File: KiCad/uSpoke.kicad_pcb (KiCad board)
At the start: 2 copper layers, 30 x 50 mm, 67 parts, among them J12 Amphenol 132289, J2 PLS-1x3, J4 PLS-1x3, Q2 AO3407A, Q3 AO3400, Q5 AO3400, U1 SP0503BAHTG, U2 TP4056, U4 LM3671MF-3.3, U5 74HC4052PW, U6 STM32F103C8T6, X1 8MHz

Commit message: Update PCB
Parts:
- removed SW5: ~, Spoke:Button_6x6
- added J1: SM12B-SRSS-TB, uSpoke:SM12B-SRSS-TB, F.Cu at (187.8, 97.5)
- added SW4: SW-SPST-2P, uSpoke:TL3330AF260QG, F.Cu at (193.4, 73.5)
- added TP1: Pad-Round, uSpoke:Pad_round, F.Cu at (161.5, 77.5)
- added TP2: Pad-Round, uSpoke:Pad_round, F.Cu at (161.5, 81.1)
- added TP3: Pad-Round, uSpoke:Pad_round, F.Cu at (161.5, 84.7)
- A1: footprint Spoke:E104-BT5005A -> uSpoke:E104-BT5005A
- A2: footprint Spoke:E22 -> uSpoke:E22
- C1, C13, C5, C8: footprint Spoke:C1206 -> uSpoke:C0805
- C11, C15, C16, C17, C18, C19, C20, C22, C23, C27, C30: footprint Spoke:C0603 -> uSpoke:C0603
- C14, C25, C26, C28: footprint Spoke:C_tantA -> uSpoke:C_tantA
- D1, D3, Q2, Q3: footprint Spoke:SOT-23 -> uSpoke:SOT-23
- D2, D4, D5: footprint Spoke:LED_3mm -> uSpoke:LED0603; moved to F.Cu
- J12: footprint Spoke:SMA -> uSpoke:SMA
- J2: value PLS-1x3 -> PLS-1x4; footprint Spoke:Header_1x3 -> uSpoke:Header_1x4
- J4: footprint Spoke:Header_1x3 -> uSpoke:Header_1x3
- L1: footprint Spoke:L1616 -> uSpoke:L1616
- Q5: footprint Spoke:SOT-23 -> uSpoke:SOT-23; moved to F.Cu
- R1, R10, R11, R12, R13, R17, R23, R26, R27, R28, R29, R3, R32, R33, R34, R5, R6, R7, R8, R9: footprint Spoke:R0603 -> uSpoke:R0603
- R15: footprint Spoke:R0603 -> uSpoke:R0603; moved to F.Cu
- R4: value 3.9kR -> 2.0kR; footprint Spoke:R0603 -> uSpoke:R0603
- SW1, SW2, SW3: value ~ -> SW-SPST-2P; footprint Spoke:Button_6x6 -> uSpoke:TL3330AF260QG
- TP10, TP11: footprint Spoke:Pad_round -> uSpoke:Pad_round
- U1: footprint Spoke:SOT-23-5 -> uSpoke:SOT-143
- U2: value TP4056 -> MCP73831T-2ACI/OT; footprint Spoke:SOIC-8-EP -> uSpoke:SOT-23-5
- U4: footprint Spoke:SOT-23-5 -> uSpoke:SOT-23-5
- U5: footprint Spoke:TSSOP-16 -> uSpoke:TSSOP-16
- U6: footprint Spoke:LQFP-48 -> uSpoke:LQFP-48
- X1: footprint Spoke:Xtal_3225 -> uSpoke:Xtal_3225
- moved SW1 197.9 mm to (193.5, 64.3), turned to 90 degrees
- moved R12 195.5 mm to (174.5, 111.0), turned to 180 degrees
- moved SW2 193.3 mm to (193.5, 55.1), turned to 90 degrees
- moved SW3 170.3 mm to (175.4, 20.6)
- moved R3 157.2 mm to (199.5, 67.6)
- moved R5 157.2 mm to (199.5, 70.2)
- moved C28 144.0 mm to (188.5, 108.1)
- moved C30 144.0 mm to (191.0, 108.8)
- moved R6 140.7 mm to (182.8, 85.2), turned to -90 degrees
- moved R1 139.0 mm to (174.5, 109.5)
- moved J2 122.6 mm to (167.1, 95.1), turned to 90 degrees
- moved R15 106.1 mm to (184.9, 92.5), turned to -90 degrees
- moved Q5 100.8 mm to (174.3, 106.7)
- moved D5 69.6 mm to (189.6, 53.2), turned to -90 degrees
- moved D4 63.6 mm to (188.1, 53.2), turned to -90 degrees
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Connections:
- C28 pad 1: BUZZ_P -> unconnected-(C28-Pad1)
- C28 pad 2: GND -> unconnected-(C28-Pad2)
- C30 pad 1: BUZZ_P -> unconnected-(C30-Pad1)
- C30 pad 2: GND -> unconnected-(C30-Pad2)
- J2 pad 1: CONSOLE_TXD_EXT -> unconnected-(J2-Pad1)
- J2 pad 2: CONSOLE_RXD_EXT -> unconnected-(J2-Pad2)
- J2 pad 3: GND -> unconnected-(J2-Pad3)
- R4 pad 1: GND -> Net-(U2-PROG)
- R4 pad 2: Net-(U2-PROG) -> GND
- SW1 pad 1: Net-(D1-Pad3) -> BUZZ_P
- SW1 pad 2: Net-(D1-Pad3) -> unconnected-(SW1-Pad2)
- SW1 pad 3: GND -> unconnected-(SW1-1-Pad3)
- SW1 pad 4: GND -> BOOT0
- SW2 pad 2: BTN_OK -> GND
- SW2 pad 3: GND -> unconnected-(SW2-1-Pad3)
- SW2 pad 4: GND -> unconnected-(SW2-1-Pad4)
- SW3 pad 2: BTN_ESC -> GND
- SW3 pad 3: GND -> unconnected-(SW3-1-Pad3)
- SW3 pad 4: GND -> unconnected-(SW3-1-Pad4)
- U1 pad 1: GND -> unconnected-(U1-A-Pad1)
- U1 pad 2: CONSOLE_TXD_EXT -> unconnected-(U1-K-Pad2)
- U1 pad 3: CONSOLE_RXD_EXT -> unconnected-(U1-K-Pad3)
- U1 pad 4: VEXT -> unconnected-(U1-K-Pad4)
- U2 pad 1: GND -> Net-(D2-K)
- U2 pad 2: Net-(U2-PROG) -> GND
- U2 pad 3: GND -> +BATT
- U2 pad 5: +BATT -> Net-(U2-PROG)
- U6 pad 42: unconnected-(U6-PB6-Pad42) -> I2C_SCL
- U6 pad 43: unconnected-(U6-PB7-Pad43) -> I2C_SDA
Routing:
- removed copper zone on B.Cu, net /ANT
- removed copper zone on F.Cu, net BUZZ_P
- removed copper zone on B.Cu, net VEXT
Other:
- board text removed: "+"
- board text removed: "-"
- board text removed: "B+"
- board text removed: "B-"
- board text removed: "CL"
- board text removed: "G"
- board text removed: "IO"
- board text removed: "RS"
- board text removed: "RX"
- board text removed: "TX"
- board text removed: "V"
- board text removed: "V+"
- board text removed: "V-"
- board text removed: "boot"

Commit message: Color 12P conn
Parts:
- J1: value SM12B-SRSS-TB -> Untitled
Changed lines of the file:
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@@
 		(at 184.95 92.47 -90)
 		(property "Reference" "R15"
-			(at 0 -1.43 -90)
+			(at 0 -1.43 270)
 			(layer "F.SilkS")
 			(effects
@@
 		)
 		(property "Value" "100kR"
-			(at 0 1.43 -90)
+			(at 0 1.43 270)
 			(layer "F.Fab")
 			(effects
@@
 		)
 		(property "Datasheet" ""
-			(at 0 0 -90)
+			(at 0 0 270)
 			(layer "F.Fab")
 			(hide yes)
@@
 		)
 		(property "Description" ""
-			(at 0 0 -90)
+			(at 0 0 270)
 			(layer "F.Fab")
 			(hide yes)
@@
 			)
 		)
-		(property "Value" "SM12B-SRSS-TB"
+		(property "Value" "Untitled"
 			(at 0.2 8.9 0)
 			(unlocked yes)

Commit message: SCH to PCB sync
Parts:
- removed C20, C22, C23, C27, C30: 100nF, uSpoke:C0603
- removed C25, C26, C28: 47uF, uSpoke:C_tantA
- removed J12: Amphenol 132289, uSpoke:SMA
- removed Q5: AO3400, uSpoke:SOT-23
- removed R23, R28, R32, R33, R34: 100kR, uSpoke:R0603
- removed R26, R27, R29: 1kR, uSpoke:R0603
- removed SW4: SW-SPST-2P, uSpoke:TL3330AF260QG
- removed TP10, TP11: Pad-Round, uSpoke:Pad_round
- removed U6: STM32F103C8T6, uSpoke:LQFP-48
- added C10: 100nF, uSpoke:C0603, F.Cu at (123.5, 60.8)
- added C12: 100nF, uSpoke:C0603, F.Cu at (123.5, 63.4)
- added C2: 47uF, uSpoke:C_tantA, F.Cu at (134.1, 75.1)
- added C3: 10uF, uSpoke:C0805, F.Cu at (132.5, 58.4)
- added C4: 10uF, uSpoke:C0805, F.Cu at (132.5, 61.4)
- added C6: 10uF, uSpoke:C0805, F.Cu at (132.5, 64.4)
- added C7: 10uF, uSpoke:C0805, F.Cu at (132.5, 67.4)
- added C9: 12pF, uSpoke:C0603, F.Cu at (123.5, 58.2)
- added J3: PLS-1x3, uSpoke:Header_1x3, F.Cu at (135.4, 71.0)
- added Q1: AO3407A, uSpoke:SOT-23, F.Cu at (140.1, 75.8)
- added R14: 1kR, uSpoke:R0603, F.Cu at (123.5, 68.6)
- added R16: 100kR, uSpoke:R0603, F.Cu at (123.5, 71.2)
- added R18: 100kR, uSpoke:R0603, F.Cu at (127.9, 58.2)
- added R19: 100kR, uSpoke:R0603, F.Cu at (127.9, 60.8)
- added R2: 100kR, uSpoke:R0603, F.Cu at (123.5, 66.0)
- added R20: 100kR, uSpoke:R0603, F.Cu at (127.9, 63.4)
- added R21: 1kR, uSpoke:R0603, F.Cu at (127.9, 66.0)
- added R22: 1kR, uSpoke:R0603, F.Cu at (127.9, 68.6)
- added TP4: Pad-Round, uSpoke:Pad_round, F.Cu at (136.7, 58.7)
- added TP5: Pad-Round, uSpoke:Pad_round, F.Cu at (136.7, 62.3)
- added U3: MCP73831T-2ACI/OT, uSpoke:SOT-23-5, F.Cu at (124.6, 75.0)
- C1, C5: value 10uF -> 100nF; footprint uSpoke:C0805 -> uSpoke:C0603
- C13: value 10uF -> 12pF; footprint uSpoke:C0805 -> uSpoke:C0603
- C15, C19: value 12pF -> 100nF
- C18: value 100nF -> 47uF; footprint uSpoke:C0603 -> uSpoke:C_tantA
- C8: value 10uF -> 47uF; footprint uSpoke:C0805 -> uSpoke:C_tantA
- J1: value Untitled -> PLS-1x4; footprint uSpoke:SM12B-SRSS-TB -> uSpoke:Header_1x4
- J2: value PLS-1x4 -> SM12B-SRSS-TB; footprint uSpoke:Header_1x4 -> uSpoke:SM12B-SRSS-TB
- J4: value PLS-1x3 -> SMA; footprint uSpoke:Header_1x3 -> uSpoke:SMA
- Q2: value AO3407A -> AO3400
- R11, R3, R8: value 0R -> 100kR
- R12: value 1kR -> 0R
- R13, R6, R7: value 100kR -> 0R
- R4: value 2.0kR -> 100kR
- R5: value 0R -> 1kR
- R9: value 100kR -> 2.0kR
- SW1, SW2, SW3: value SW-SPST-2P -> TL3330AF260QG
- U2: value MCP73831T-2ACI/OT -> LM3671MF-3.3
- U4: value LM3671MF-3.3 -> 74HC4052PW; footprint uSpoke:SOT-23-5 -> uSpoke:TSSOP-16
- U5: value 74HC4052PW -> STM32F103C8T6; footprint uSpoke:TSSOP-16 -> uSpoke:LQFP-48
- moved J2 23.4 mm to (188.7, 104.1), turned to 0 degrees
- moved U4 12.3 mm to (199.1, 82.7)
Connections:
- A1 pad 4: BUZZ_P -> +3V3
- A2 pad 9: BUZZ_P -> +3V3
- C1 pad 1: GND -> +3V3
- C1 pad 2: VEXT -> GND
- C11 pad 1: BUZZ_P -> +3V3
- C13 pad 1: GND -> Net-(U5-PD1)
- C13 pad 2: BUZZ_P -> GND
- C14 pad 1: BUZZ_P -> +3V3
- C15 pad 1: Net-(U6-PD0) -> +3V3
- C16 pad 1: BUZZ_P -> +3V3
- C17 pad 1: BUZZ_P -> +3V3
- C18 pad 1: BUZZ_P -> +3V3
- C19 pad 1: Net-(U6-PD1) -> VBAT_SENSE
- C5 pad 1: GND -> +3V3
- C5 pad 2: +BATT -> GND
- C8 pad 1: GND -> +3V3
- C8 pad 2: VCC -> GND
- D1 pad 1: Net-(Q2-G) -> Net-(Q1-G)
- D3 pad 1: BUZZ_N -> BUZZER_N
- D3 pad 2: BUZZ_N -> BUZZER_N
- D3 pad 3: BUZZ_P -> +3V3
- J1 pad 1: unconnected-(J1-Pad1) -> VBUS
- J1 pad 2: unconnected-(J1-Pad2) -> CONSOLE_TXD_EXT
- J1 pad 3: unconnected-(J1-Pad3) -> CONSOLE_RXD_EXT
- J1 pad 4: unconnected-(J1-Pad4) -> GND
- J2 pad 1: unconnected-(J2-Pad1) -> BUZZER_N
- J2 pad 2: unconnected-(J2-Pad2) -> +3V3
- J2 pad 3: unconnected-(J2-Pad3) -> MOVE_SW
- J2 pad 4: unconnected-(J2-Pad4) -> GND
- J4 pad 1: SWD_CLK -> /ANT
- J4 pad 2: SWD_IO -> GND
- L1 pad 1: Net-(U4-SW) -> Net-(U2-SW)
- L1 pad 2: BUZZ_P -> +3V3
- Q2 pad 1: Net-(Q2-G) -> PWR_HOLD
- Q2 pad 2: +BATT -> GND
- Q2 pad 3: VCC -> Net-(Q1-G)
- Q3 pad 1: PWR_HOLD -> Net-(Q3-G)
- Q3 pad 3: Net-(Q2-G) -> BUZZER_N
- R1 pad 1: Net-(Q5-G) -> +BATT
- R1 pad 2: GND -> Net-(Q1-G)
- R10 pad 1: Net-(D2-A) -> BUZZER_PWM
- R10 pad 2: VEXT -> Net-(Q3-G)
- R11 pad 1: CONSOLE_RXD -> Net-(Q3-G)
- R11 pad 2: BLE_TXD -> GND
- R12 pad 1: BUZZER -> CONSOLE_TXD
- R12 pad 2: Net-(Q5-G) -> BLE_RXD
- R13 pad 1: BUZZ_P -> CONSOLE_RXD
- R13 pad 2: MUX_BLE_EXT -> BLE_TXD
- R15 pad 2: BUZZ_P -> +3V3
- R17 pad 1: BOOT0 -> +3V3
- R17 pad 2: GND -> Net-(A1-nRESET)
- R3 pad 1: CONSOLE_TXD -> BOOT0/BTN_ESC
- R3 pad 2: CONSOLE_TXD_EXT -> GND
- R4 pad 1: Net-(U2-PROG) -> BOOT1
- R5 pad 1: CONSOLE_RXD -> Net-(D2-A)
- R5 pad 2: CONSOLE_RXD_EXT -> VBUS
- R6 pad 1: BOOT1 -> CONSOLE_TXD
- R6 pad 2: GND -> CONSOLE_TXD_EXT
- R7 pad 1: +BATT -> CONSOLE_RXD
- R7 pad 2: Net-(Q2-G) -> CONSOLE_RXD_EXT
- R8 pad 1: CONSOLE_TXD -> +3V3
- R8 pad 2: BLE_RXD -> MUX_BLE_EXT
- R9 pad 1: GND -> Net-(U3-PROG)
- R9 pad 2: PWR_HOLD -> GND
- SW1 pad 1: BUZZ_P -> Net-(D1-Pad3)
- SW1 pad 2: unconnected-(SW1-Pad2) -> GND
- SW1 pad 3: unconnected-(SW1-1-Pad3) -> GND
- SW1 pad 4: BOOT0 -> GND
- SW2 pad 3: unconnected-(SW2-1-Pad3) -> GND
- SW2 pad 4: unconnected-(SW2-1-Pad4) -> GND
- SW3 pad 1: BTN_ESC -> +3V3
- SW3 pad 2: GND -> BOOT0/BTN_ESC
- SW3 pad 3: unconnected-(SW3-1-Pad3) -> GND
- SW3 pad 4: unconnected-(SW3-1-Pad4) -> GND
- TP1 pad 1: I2C_SDA -> Net-(A1-SWDIO)
- TP2 pad 1: I2C_SCL -> Net-(A1-SWDCLK)
- TP3 pad 1: GND -> I2C_SCL
- U1 pad 1: unconnected-(U1-A-Pad1) -> GND
- U1 pad 2: unconnected-(U1-K-Pad2) -> VBUS
- U1 pad 3: unconnected-(U1-K-Pad3) -> CONSOLE_TXD_EXT
- U1 pad 4: unconnected-(U1-K-Pad4) -> CONSOLE_RXD_EXT
- U2 pad 1: Net-(D2-K) -> VCC
- U2 pad 3: +BATT -> VCC
- U2 pad 4: VEXT -> +3V3
- U2 pad 5: Net-(U2-PROG) -> Net-(U2-SW)
- U4 pad 1: VCC -> BLE_TXD
- U4 pad 2: GND -> unconnected-(U4-2Y2-Pad2)
- U4 pad 3: VCC -> CONSOLE_RXD
- U4 pad 4: BUZZ_P -> unconnected-(U4-2Y3-Pad4)
- U4 pad 5: Net-(U4-SW) -> CONSOLE_RXD_EXT
- U5 pad 1: BLE_TXD -> +3V3
- U5 pad 10: MUX_BLE_EXT -> BUZZER_PWM
- U5 pad 11: unconnected-(U5-1Y3-Pad11) -> GPS_PPS
- U5 pad 12: BLE_RXD -> VBAT_SENSE
- U5 pad 13: CONSOLE_TXD -> RF_RESET
- U5 pad 14: CONSOLE_TXD_EXT -> RF_CS
- U5 pad 15: unconnected-(U5-1Y2-Pad15) -> RF_SCK
- U5 pad 16: BUZZ_P -> RF_MISO
- U5 pad 2: unconnected-(U5-2Y2-Pad2) -> MOVE_SW
- U5 pad 3: CONSOLE_RXD -> MUX_BLE_EXT
- U5 pad 4: unconnected-(U5-2Y3-Pad4) -> BLE_MODE
- U5 pad 5: CONSOLE_RXD_EXT -> Net-(U5-PD0)
- U5 pad 6: GND -> Net-(U5-PD1)
- U5 pad 7: GND -> MCU_RESET
- U5 pad 9: GND -> +3V3
- X1 pad 1: Net-(U6-PD0) -> Net-(U5-PD0)
- X1 pad 3: Net-(U6-PD1) -> Net-(U5-PD1)
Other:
- board text added: "Rev.1.0"
- board text added: "uSpoke"
- board text removed: "Rev.2.1"
- board text removed: "Spoke"

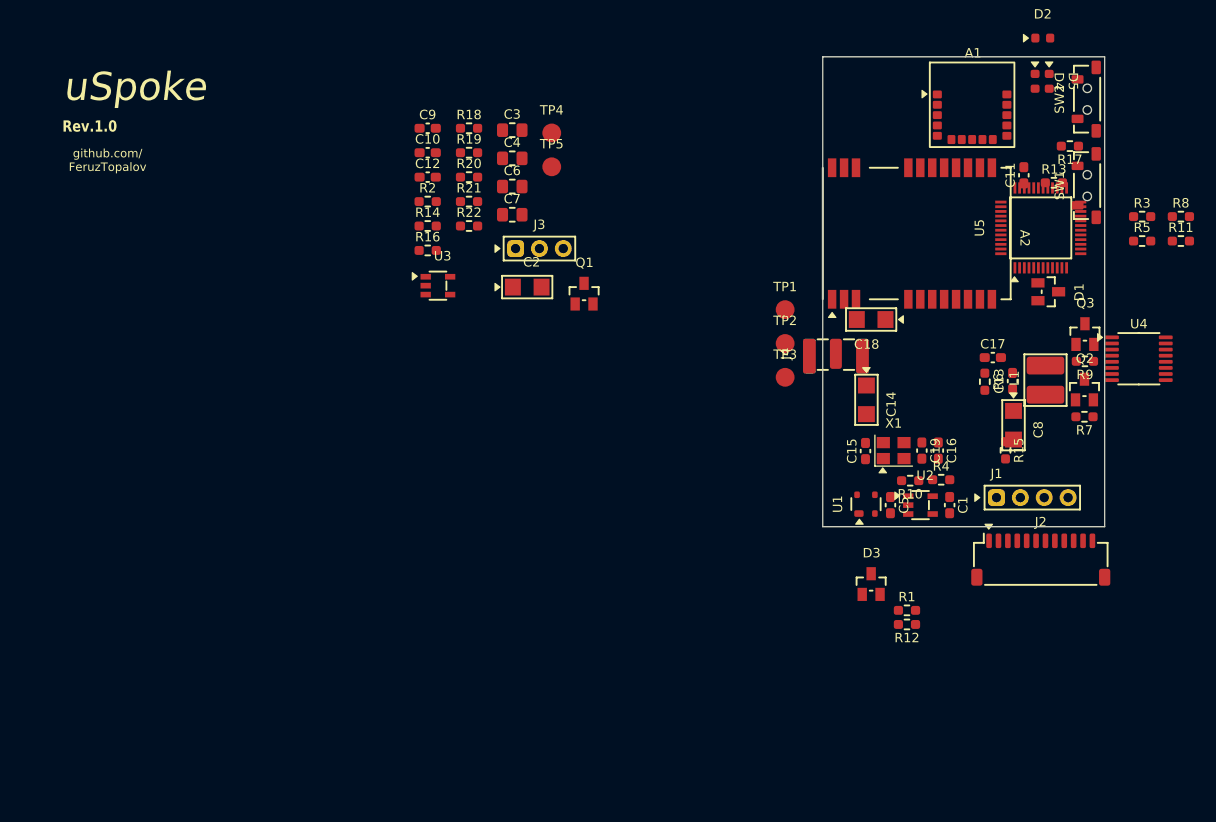
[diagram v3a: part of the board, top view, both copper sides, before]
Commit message: Reduce footprints to auto soldering
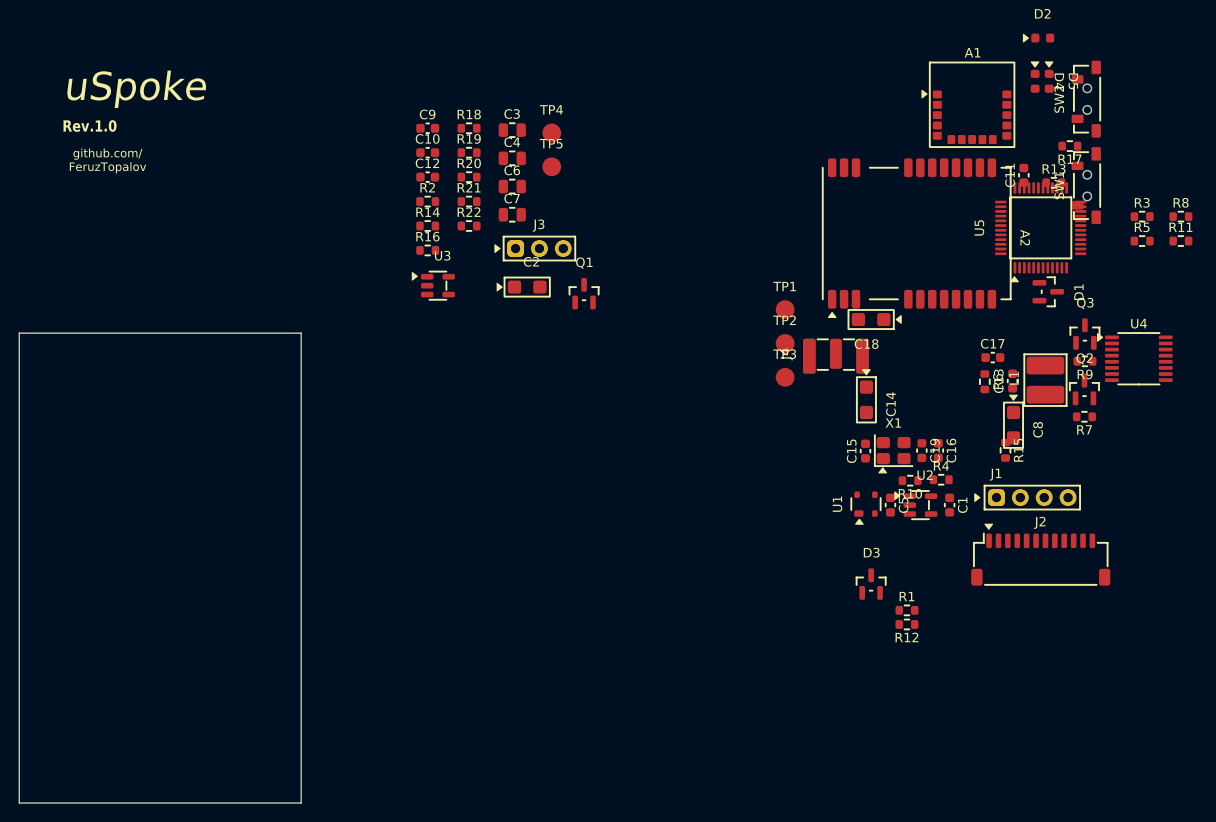
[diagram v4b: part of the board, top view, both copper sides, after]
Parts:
- J2: value SM12B-SRSS-TB -> Untitled

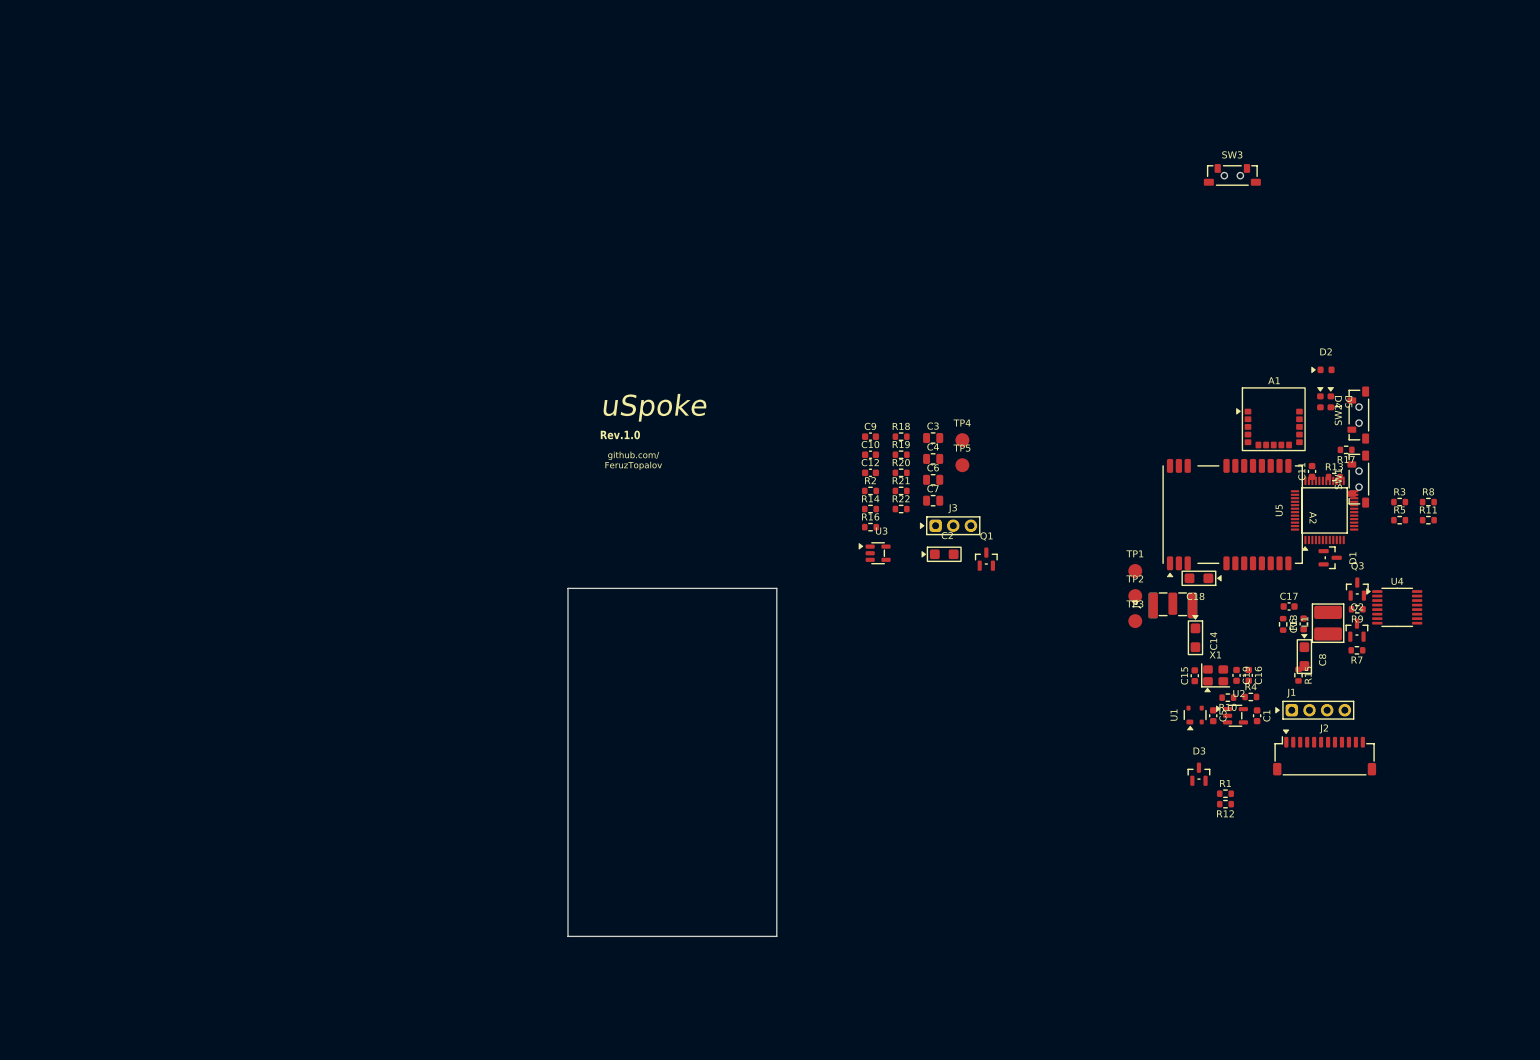
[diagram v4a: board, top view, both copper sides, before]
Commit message: PCB comps placement
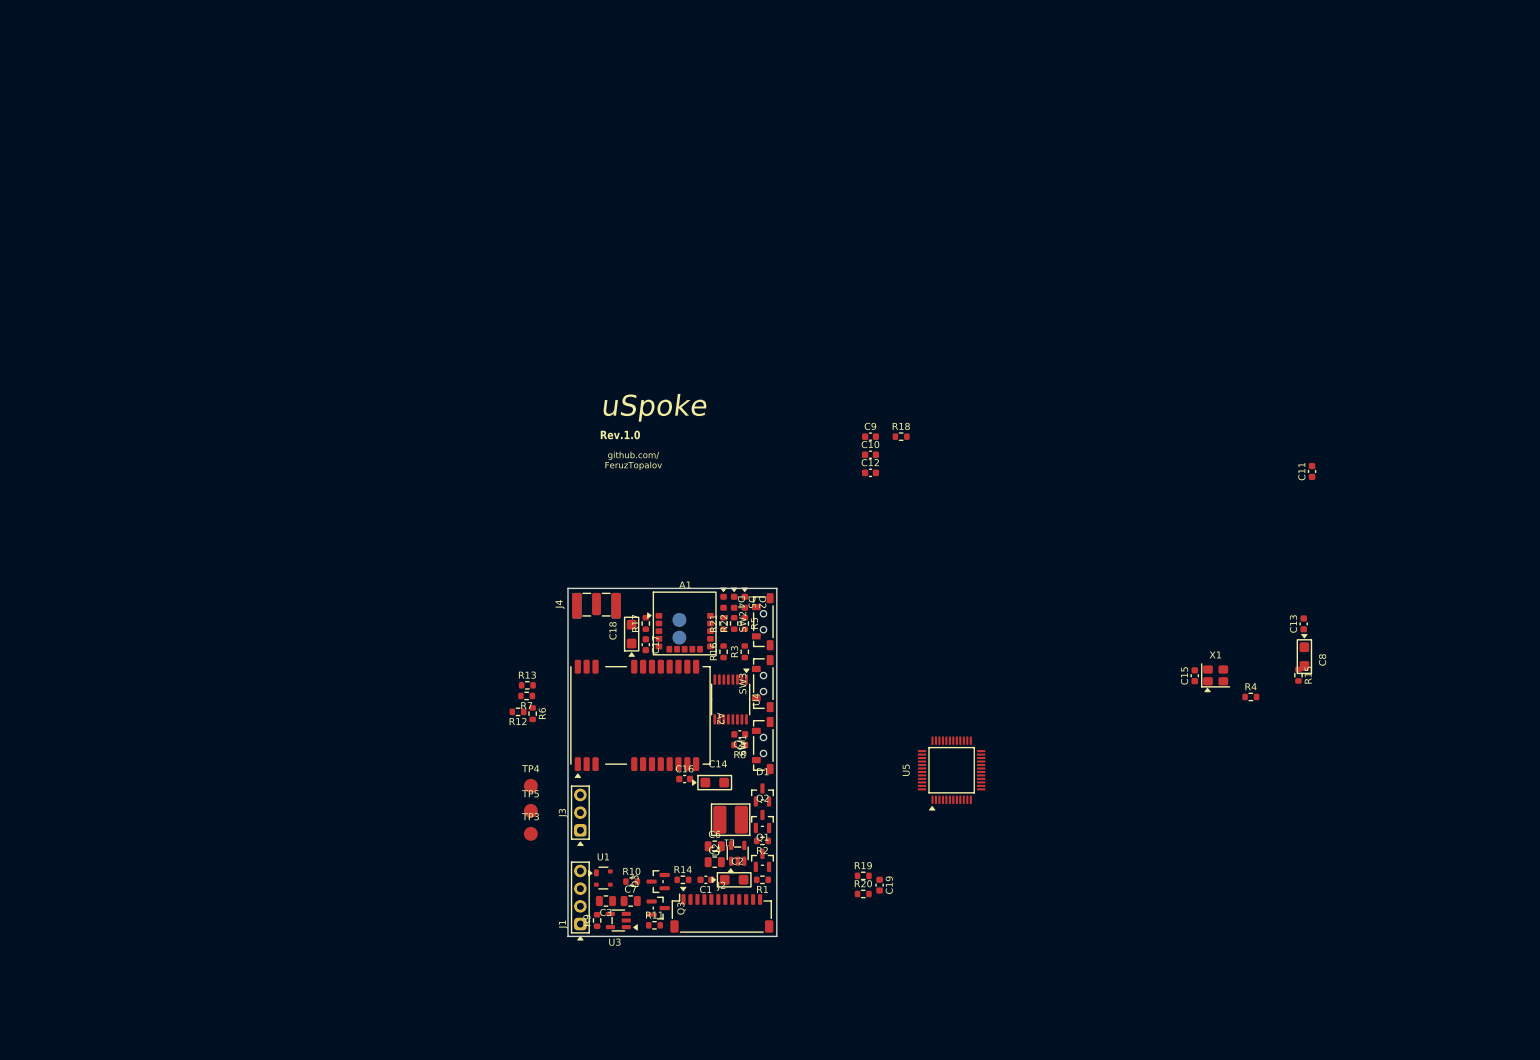
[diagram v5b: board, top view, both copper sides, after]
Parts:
- TP1, TP2: moved to B.Cu
- moved R11 125.5 mm to (92.4, 128.4)
- moved R13 119.7 mm to (74.2, 93.9)
- moved R7 119.5 mm to (74.1, 95.5)
- moved R9 118.0 mm to (84.2, 127.7), turned to 90 degrees
- moved Q3 110.4 mm to (93.0, 125.9), turned to -90 degrees
- moved J1 109.4 mm to (81.8, 124.4), turned to 90 degrees
- moved R6 108.6 mm to (74.9, 98.0)
- moved R8 104.9 mm to (104.7, 102.5), turned to 180 degrees
- moved R17 103.7 mm to (91.2, 85.0), turned to 90 degrees
- moved R12 102.5 mm to (72.8, 97.7)
- moved SW3 99.5 mm to (107.9, 93.7), turned to 90 degrees
- moved U4 96.7 mm to (103.4, 96.0), turned to -90 degrees
- moved R3 96.5 mm to (105.4, 89.1), turned to 90 degrees
- moved R5 95.3 mm to (105.4, 85.0), turned to -90 degrees
- moved SW1 93.7 mm to (107.9, 102.6)
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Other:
- rule pad_to_mask_clearance: 0.038 -> 0.05
